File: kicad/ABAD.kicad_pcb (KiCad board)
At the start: 4 copper layers, 36.9 x 85.2 mm, 58 parts, among them J1 Edge mounted SMA, J2 USB_C_Receptacle_USB2.0_16P, J3 BATT Screw Terminal, Q1 AO3401A, Q2 AO3401A, U2 ESP32-S3-WROOM-1, U3 USBLC6-2SC6, U4 TPS63001, U6 MPU-6050, U7 MS5611-01BA, U8 L80-R

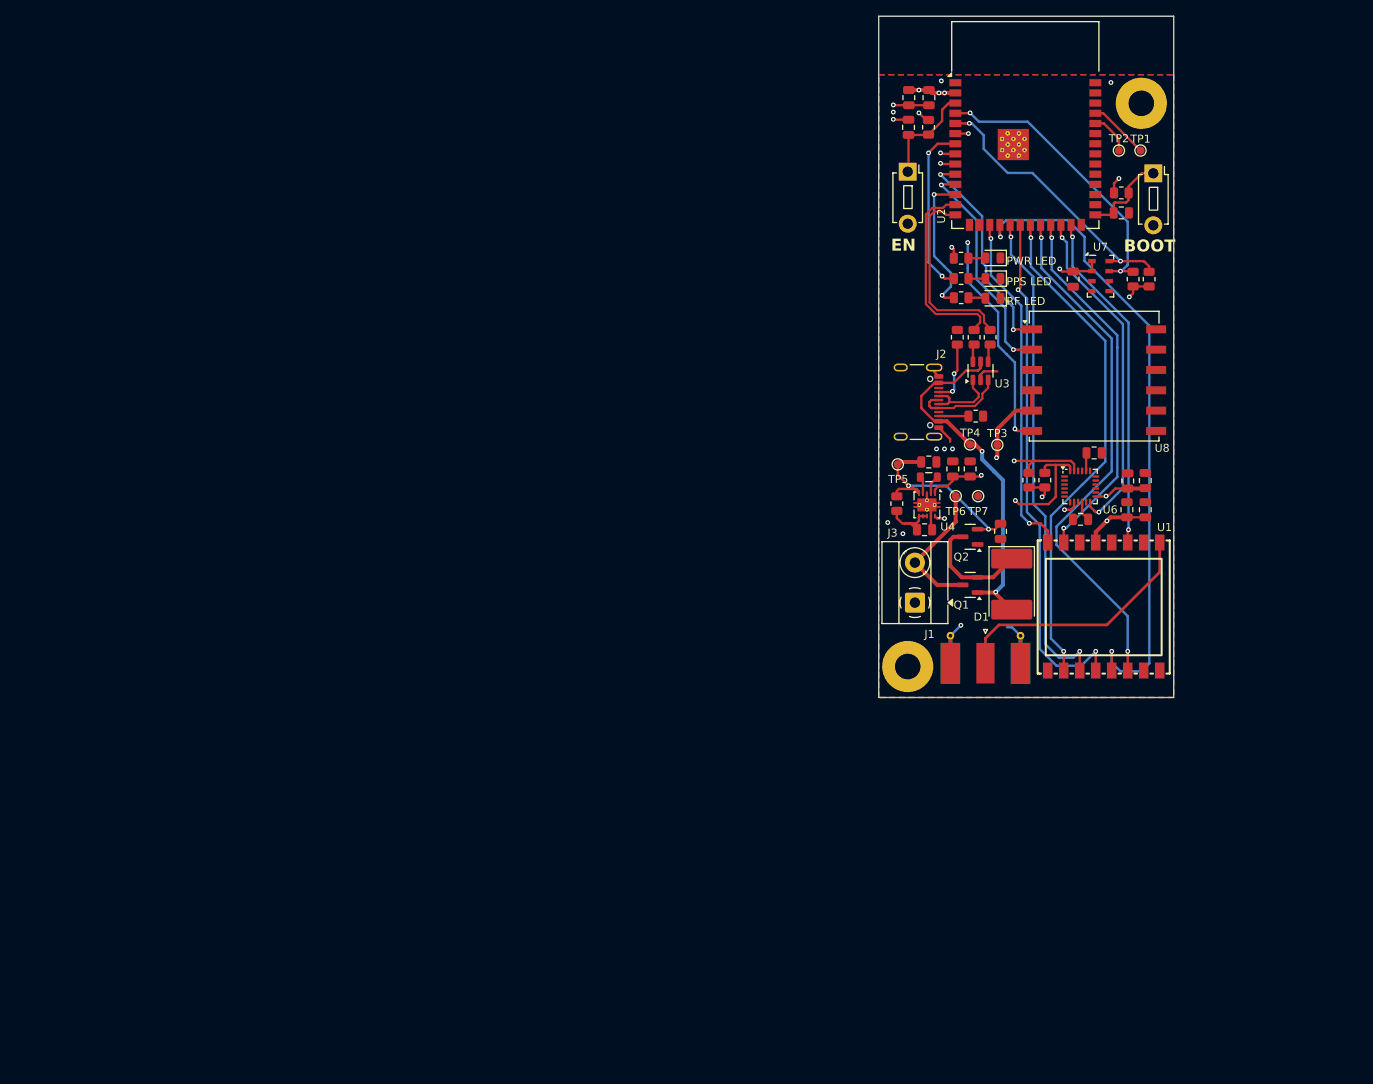
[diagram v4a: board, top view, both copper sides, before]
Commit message: Completed PCB + Sch, RP2040 based
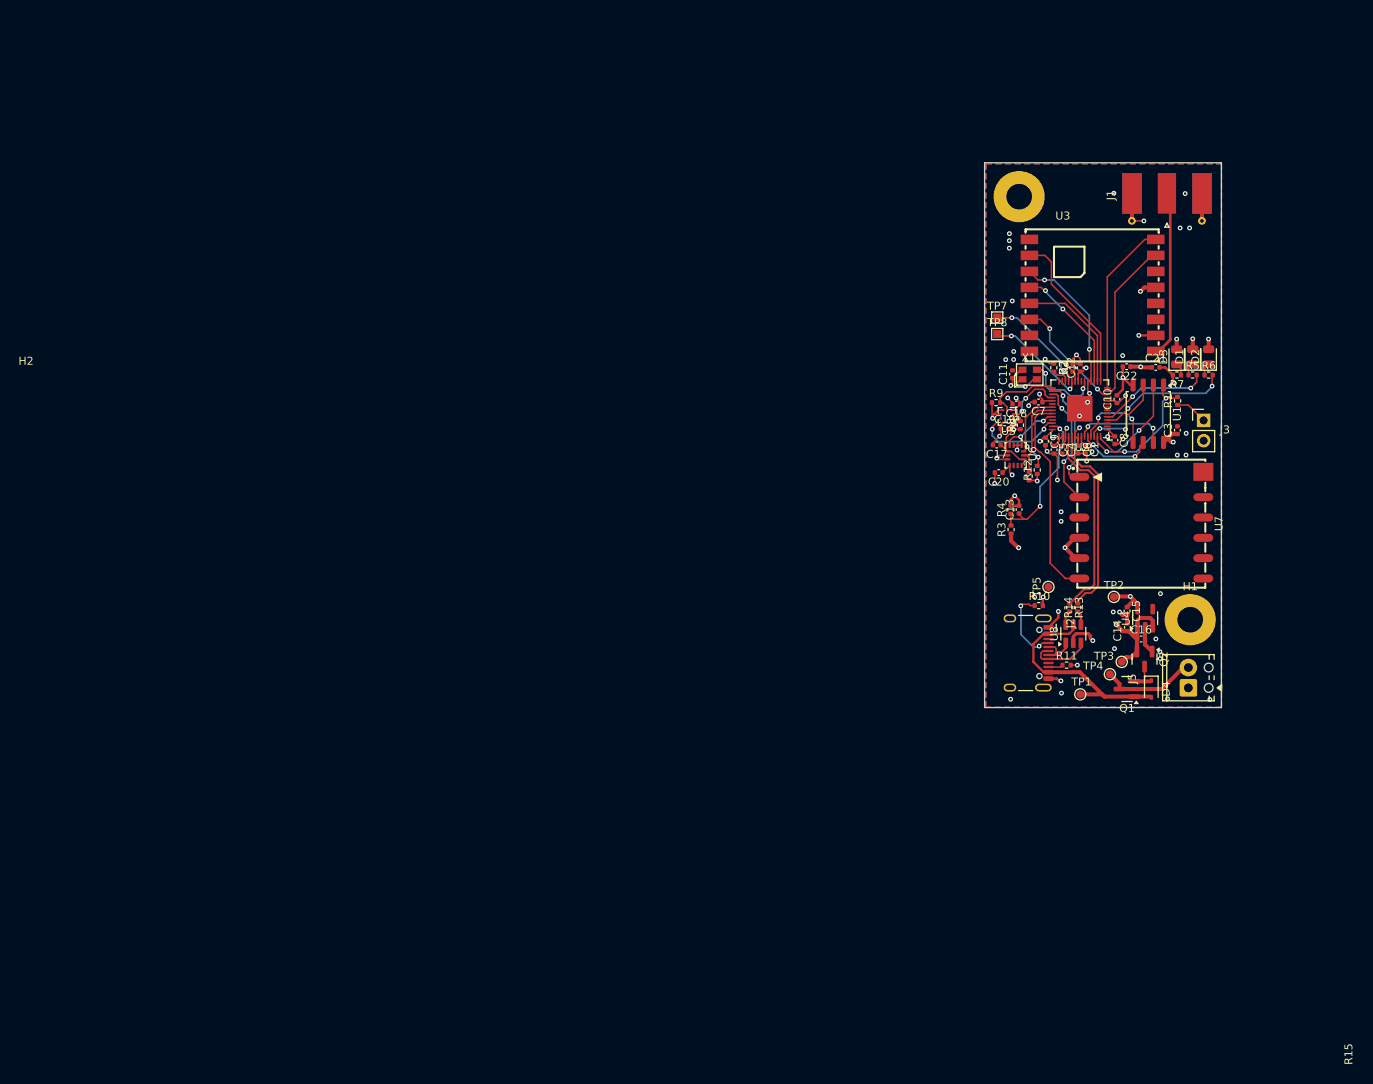
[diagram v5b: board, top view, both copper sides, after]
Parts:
- removed L1: 1.5A 2.2uH, Inductor_SMD:L_0805_2012Metric
- removed RESET_SW1, RESET_SW2: SW_Push, Button_Switch_THT:SW_PUSH_1P1T_6x3.5mm_H4.3_APEM_MJTP1243
- removed TP6: BATT_RAW+, TestPoint:TestPoint_Pad_D1.0mm
- added C19: 100nF, Capacitor_SMD:C_0402_1005Metric, F.Cu at (144.0, 94.9)
- added C20: 100nF, Capacitor_SMD:C_0402_1005Metric, F.Cu at (143.3, 100.4)
- added C21: 100nF, Capacitor_SMD:C_0402_1005Metric, F.Cu at (162.9, 87.2)
- added C22: 10uF, Capacitor_SMD:C_0402_1005Metric, F.Cu at (159.3, 87.1)
- added C5: 1uF, Capacitor_SMD:C_0402_1005Metric, F.Cu at (150.2, 97.5)
- added C6: 100nF, Capacitor_SMD:C_0402_1005Metric, F.Cu at (153.2, 97.5)
- added J5: BATT Screw Terminal, TerminalBlock_Phoenix:TerminalBlock_Phoenix_MPT-0,5-2-2.54_1x02_P2.54mm_Horizontal, F.Cu at (167.0, 127.3)
- added R15: 10k, Resistor_SMD:R_0402_1005Metric, F.Cu at (147.1, 100.8)
- added TP8: SWD, TestPoint:TestPoint_Pad_1.0x1.0mm, F.Cu at (143.1, 83.0)
- added U5: BMP390, JLC_BMP390:LGA-10_L2.0-W2.0-P0.50-TL_BMP390L, F.Cu at (144.3, 93.3)
- added X1: 12MHz, Crystal:OSC-SMD_4P-L2.0-W1.6-BL, F.Cu at (147.2, 88.1)
- C1: footprint Capacitor_SMD:C_0805_2012Metric -> Capacitor_SMD:C_0402_1005Metric
- C10, C11, C2, C9: value 10uF -> 100nF; footprint Capacitor_SMD:C_0805_2012Metric -> Capacitor_SMD:C_0402_1005Metric
- C12: value 10nF, 4V -> 100nF; footprint Capacitor_SMD:C_0805_2012Metric -> Capacitor_SMD:C_0402_1005Metric
- C13: value 0.1uF, 4V -> 100nF; footprint Capacitor_SMD:C_0805_2012Metric -> Capacitor_SMD:C_0402_1005Metric
- C14: value 100nF -> 1uF; footprint Capacitor_SMD:C_0805_2012Metric -> Capacitor_SMD:C_0402_1005Metric
- C15: value 0.1uF, 2V -> 1uF; footprint Capacitor_SMD:C_0805_2012Metric -> Capacitor_SMD:C_0402_1005Metric
- C16: value 2.2nF, 50V -> 10uF; footprint Capacitor_SMD:C_0805_2012Metric -> Capacitor_SMD:C_0402_1005Metric
- C17: value 22uF -> 100nF; footprint Capacitor_SMD:C_0805_2012Metric -> Capacitor_SMD:C_0402_1005Metric
- C18, C8: value 0.1uF -> 100nF; footprint Capacitor_SMD:C_0805_2012Metric -> Capacitor_SMD:C_0402_1005Metric
- C3: value 10uF 6.3V -> 100nF; footprint Capacitor_SMD:C_0805_2012Metric -> Capacitor_SMD:C_0402_1005Metric
- C4: value 0.1uF -> 1uF; footprint Capacitor_SMD:C_0805_2012Metric -> Capacitor_SMD:C_0402_1005Metric
- C7: value 1uF -> 100nF; footprint Capacitor_SMD:C_0805_2012Metric -> Capacitor_SMD:C_0402_1005Metric
- D1: value D_Schottky -> RF_LED_GREEN; footprint Diode_SMD:D_3220_8050Metric -> LED_SMD:LED_0805_2012Metric
- D2: value RF_LED_GREEN -> GPS_LED_BLUE
- D3: value GPS_LED_BLUE -> PWR_LED_RED
- D4: value PWR_LED_RED -> D_Schottky; footprint LED_SMD:LED_0805_2012Metric -> Diode_SMD:D_SOD-323
- J2: footprint Connector_USB:USB_C_Receptacle_GCT_USB4105-xx-A_16P_TopMnt_Horizontal -> Connector_USB:USB_C_Receptacle_HCTL_HC-TYPE-C-16P-01A
- J3: value BATT Screw Terminal -> Conn_01x02; footprint TerminalBlock_MetzConnect:TerminalBlock_MetzConnect_Type055_RT01502HDWU_1x02_P5.00mm_Horizontal -> Connector_PinHeader_2.54mm:PinHeader_1x02_P2.54mm_Vertical
- R1: value 5.1k -> 1k; footprint Resistor_SMD:R_0805_2012Metric -> Resistor_SMD:R_0402_1005Metric
- R10: value 68 -> 5.1k; footprint Resistor_SMD:R_0805_2012Metric -> Resistor_SMD:R_0402_1005Metric
- R11: value 10k -> 5.1k; footprint Resistor_SMD:R_0805_2012Metric -> Resistor_SMD:R_0402_1005Metric
- R12, R2: footprint Resistor_SMD:R_0805_2012Metric -> Resistor_SMD:R_0402_1005Metric
- R13, R14: value 10k -> 22Ω; footprint Resistor_SMD:R_0805_2012Metric -> Resistor_SMD:R_0402_1005Metric
- R3: value 100Ω -> 30k; footprint Resistor_SMD:R_0805_2012Metric -> Resistor_SMD:R_0402_1005Metric
- R4: value 22Ω -> 51k; footprint Resistor_SMD:R_0805_2012Metric -> Resistor_SMD:R_0402_1005Metric
- R5: value 22Ω -> 1k; footprint Resistor_SMD:R_0805_2012Metric -> Resistor_SMD:R_0402_1005Metric
- R6, R7: value 10k -> 1k; footprint Resistor_SMD:R_0805_2012Metric -> Resistor_SMD:R_0402_1005Metric
- R8, R9: value 68 -> 4.7k; footprint Resistor_SMD:R_0805_2012Metric -> Resistor_SMD:R_0402_1005Metric
- TP1: value TXD0 -> VBUS
- TP2: value RXD0 -> 3.3V
- TP3: value 3.3V -> BATT+
- TP4: value VBUS -> BATT_RAW+
- TP5: value BATT+ -> GND
- TP7: value GND -> SWCLK; footprint TestPoint:TestPoint_Pad_D1.0mm -> TestPoint:TestPoint_Pad_1.0x1.0mm
- U1: value ~ -> W25Q128JVS; footprint Lora1262:WIRELM-SMD_16P-L16.0-W16.0-P2.00_LORA-CC68-915MHZ-TCXO -> Package_SO:SOIC-8_5.3x5.3mm_P1.27mm
- U2: value ESP32-S3-WROOM-1 -> RP2040; footprint RF_Module:ESP32-S3-WROOM-1 -> Package_DFN_QFN:QFN-56-1EP_7x7mm_P0.4mm_EP3.2x3.2mm
- U3: value USBLC6-2SC6 -> 433MHz; footprint Package_TO_SOT_SMD:SOT-23-6 -> LORA-CC68-433MHz-TCXO:LCC-16_L16.0-W16.0-P2.00-TL
- U4: value TPS63001 -> AP2112K-3.3; footprint Package_SON:Texas_DRC0010J_ThermalVias -> Package_TO_SOT_SMD:SOT-23-5
- U6: value MPU-6050 -> LSMDSO32TR; footprint Sensor_Motion:InvenSense_QFN-24_4x4mm_P0.5mm -> LSMDSO32TR:LGA-14_L3.0-W2.5-P0.50-TL
- U7: value MS5611-01BA -> L80RE-M37; footprint Package_LGA:LGA-8_3x5mm_P1.25mm -> L80RE-M37:GPSM-SMD_12P-L16.0-W16.0-P2.54-BL
- U8: value L80-R -> USBLC6-2SC6; footprint RF_GPS:Quectel_L80-R -> Package_TO_SOT_SMD:SOT-23-6
- moved TP1 68.4 mm to (153.5, 128.1)
- moved J1 59.8 mm to (164.3, 67.2), turned to -90 degrees
- moved D4 57.4 mm to (162.3, 127.4), turned to -90 degrees
- moved TP2 55.8 mm to (157.7, 115.9)
- moved R11 49.0 mm to (151.8, 124.4), turned to 0 degrees
- moved R6 46.7 mm to (169.5, 88.2), turned to 0 degrees
- moved C17 44.8 mm to (143.0, 96.9), turned to 180 degrees
- moved R10 44.5 mm to (148.3, 117.0), turned to 0 degrees
- moved C14 44.1 mm to (159.4, 119.7), turned to 90 degrees
- moved J3 42.7 mm to (168.9, 93.8), turned to 0 degrees
- moved C18 39.8 mm to (145.5, 91.8), turned to 180 degrees
- moved C7 38.0 mm to (148.2, 91.5), turned to 180 degrees
- moved D1 36.3 mm to (167.5, 85.9), turned to 90 degrees
- moved U2 36.1 mm to (153.4, 92.4), turned to 180 degrees
- moved H1 35.8 mm to (167.2, 118.8)
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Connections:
- C1 pad 1: GND -> +1V1
- C1 pad 2: +3.3V -> GND
- C10 pad 1: +BATT -> +3V3
- C11 pad 1: +3.3V -> +3V3
- C12 pad 1: GND -> +3V3
- C12 pad 2: +3.3V -> GND
- C13 pad 1: +3.3V -> /BATT SENSE
- C14 pad 1: +3.3V -> +BATT
- C15 pad 1: Net-(U6-REGOUT) -> +3V3
- C16 pad 1: Net-(U6-CPOUT) -> +BATT
- C17 pad 1: GND -> +3V3
- C17 pad 2: +3.3V -> GND
- C18 pad 2: +3.3V -> +3V3
- C2 pad 1: GND -> +1V1
- C2 pad 2: +3.3V -> GND
- C3 pad 1: +BATT -> +3V3
- C4 pad 1: Net-(U4-EN) -> +1V1
- C7 pad 1: GND -> +3V3
- C7 pad 2: /EN_RST -> GND
- C8 pad 1: GND -> +3V3
- C8 pad 2: /BOOT -> GND
- C9 pad 1: +3.3V -> +3V3
- D1 pad 2: VBUS -> +3V3
- D2 pad 1: GND -> Net-(D2-K)
- D2 pad 2: Net-(D2-A) -> +3V3
- D3 pad 1: GND -> Net-(D3-K)
- D3 pad 2: Net-(D3-A) -> +3V3
- D4 pad 1: GND -> Net-(D4-K)
- D4 pad 2: Net-(D4-A) -> VBUS
- J2 pad A6: USB+ -> Net-(J2-D+-PadA6)
- J2 pad A7: USB- -> Net-(J2-D--PadA7)
- J2 pad B6: USB+ -> Net-(J2-D+-PadA6)
- J2 pad B7: USB- -> Net-(J2-D--PadA7)
- J3 pad 1: GND -> /BOOTSEL
- J3 pad 2: BATT_RAW+ -> GND
- Q1 pad 2: Net-(D1-K) -> Net-(D4-K)
- Q1 pad 3: BATT_RAW+ -> RAW_BATT+
- Q2 pad 3: Net-(D1-K) -> Net-(D4-K)
- R1 pad 1: Net-(J2-CC1) -> /BOOTSEL
- R1 pad 2: GND -> /QSPI_SS
- R10 pad 1: Net-(D4-A) -> Net-(J2-CC1)
- R10 pad 2: +3.3V -> GND
- R11 pad 1: +3.3V -> Net-(J2-CC2)
- R11 pad 2: /BARO_SDA -> GND
- R12 pad 1: +3.3V -> +3V3
- R12 pad 2: /BARO_SCL -> /ACCEL_SDA
- R13 pad 1: +3.3V -> /USB_D-
- R13 pad 2: /ACCEL_SDA -> Net-(R13-Pad2)
- R14 pad 1: +3.3V -> Net-(R14-Pad1)
- R14 pad 2: /ACCEL_SCL -> /USB_D+
- R2 pad 1: Net-(J2-CC2) -> +3V3
- R2 pad 2: GND -> /RUN
- R3 pad 2: Net-(U4-EN) -> /BATT SENSE
- R4 pad 1: USBN -> /BATT SENSE
- R4 pad 2: Net-(R4-Pad2) -> GND
- R5 pad 1: Net-(R5-Pad1) -> Net-(D1-K)
- R5 pad 2: USBP -> /RF_LED
- R6 pad 1: /EN_RST -> Net-(D2-K)
- R6 pad 2: +3.3V -> /PPS_LED
- R7 pad 1: /BOOT -> Net-(D3-K)
- R7 pad 2: +3.3V -> GND
- R8 pad 1: Net-(D2-A) -> +3V3
- R8 pad 2: /RF_LED -> /BMP_SCL
- R9 pad 1: Net-(D3-A) -> +3V3
- R9 pad 2: /PPS_LED -> /BMP_SDA
- TP1 pad 1: /TXD0 -> VBUS
- TP2 pad 1: /RXD0 -> +3V3
- TP3 pad 1: +3.3V -> +BATT
- TP4 pad 1: VBUS -> RAW_BATT+
- TP5 pad 1: +BATT -> GND
- TP7 pad 1: GND -> /SWD
- U1 pad 1: GND -> /QSPI_SS
- U1 pad 2: /MISO -> /QSPI_SD1
- U1 pad 3: /MOSI -> /QSPI_SD2
- U1 pad 4: /SCLK -> GND
- U1 pad 5: /NSS -> /QSPI_SD0
- U1 pad 6: /NRESET -> /QSPI_SCLK
- U1 pad 7: unconnected-(U1-NC-Pad7) -> /QSPI_SD3
- U1 pad 8: GND -> +3V3
- U2 pad 1: GND -> +3V3
- U2 pad 10: /GPS_RX -> +3V3
- U2 pad 11: /GPS_TX -> unconnected-(U2-GPIO8-Pad11)
- U2 pad 12: /RF_LED -> /RESET
- U2 pad 13: USBN -> /DIO1
- U2 pad 14: USBP -> /BUSY
- U2 pad 15: unconnected-(U2-IO3-Pad15) -> /MISO
- U2 pad 16: unconnected-(U2-IO46-Pad16) -> /NSS
- U2 pad 17: /BUSY -> /SCK
- U2 pad 18: /NSS -> /MOSI
- U2 pad 19: /MOSI -> GND
- U2 pad 2: +3.3V -> unconnected-(U2-GPIO0-Pad2)
- U2 pad 20: /SCLK -> /XIN
- U2 pad 21: /MISO -> unconnected-(U2-XOUT-Pad21)
- U2 pad 22: /NRESET -> +3V3
- U2 pad 23: /TXCO -> +1V1
- U2 pad 24: /ACCEL_INT -> /SWCLK
- U2 pad 25: /RF_INT -> /SWD
- U2 pad 26: unconnected-(U2-IO45-Pad26) -> /RUN
- U2 pad 27: /BOOT -> unconnected-(U2-GPIO16-Pad27)
- U2 pad 29: unconnected-(U2-IO36-Pad29) -> /BMP_SDA
- U2 pad 3: /EN_RST -> unconnected-(U2-GPIO1-Pad3)
- U2 pad 30: unconnected-(U2-IO37-Pad30) -> /GPS_RX
- U2 pad 31: unconnected-(U2-IO38-Pad31) -> /GPS_TX
- U2 pad 32: unconnected-(U2-IO39-Pad32) -> /BMP_SCL
- U2 pad 33: unconnected-(U2-IO40-Pad33) -> +3V3
- U2 pad 35: unconnected-(U2-IO42-Pad35) -> /ACCEL_SDA
- U2 pad 36: /RXD0 -> /ACCEL_SCL
- U2 pad 37: /TXD0 -> /PPS
- U2 pad 38: unconnected-(U2-IO2-Pad38) -> /ACCEL_INT
- U2 pad 4: /BARO_SDA -> /PPS_LED
- U2 pad 40: GND -> /BMP_INT
- U2 pad 41: GND -> /BATT SENSE
- U2 pad 5: /BARO_SCL -> /RF_LED
- U2 pad 6: /PPS -> unconnected-(U2-GPIO4-Pad6)
- U2 pad 7: /PPS_LED -> unconnected-(U2-GPIO5-Pad7)
- U2 pad 8: /ACCEL_SDA -> unconnected-(U2-GPIO6-Pad8)
- U2 pad 9: /ACCEL_SCL -> unconnected-(U2-GPIO7-Pad9)
- U3 pad 1: USB- -> GND
- U3 pad 2: GND -> /MISO
- U3 pad 3: USB+ -> /MOSI
- U3 pad 4: Net-(R5-Pad1) -> /SCK
- U3 pad 5: VBUS -> /NSS
- U3 pad 6: Net-(R4-Pad2) -> /RESET
- U4 pad 1: +3.3V -> +BATT
- U4 pad 2: Net-(U4-L2) -> GND
- U4 pad 3: GND -> +BATT
- U4 pad 4: Net-(U4-L1) -> unconnected-(U4-NC-Pad4)
- U4 pad 5: +BATT -> +3V3
- U6 pad 1: unconnected-(U6-CLKIN-Pad1) -> GND
- U6 pad 10: Net-(U6-REGOUT) -> unconnected-(U6-NC-Pad10)
- U6 pad 11: GND -> unconnected-(U6-NC-Pad11)
- U6 pad 12: /ACCEL_INT -> +3V3
- U6 pad 13: +3.3V -> /ACCEL_SCL
- U6 pad 14: unconnected-(U6-NC-Pad14) -> /ACCEL_SDA
- U6 pad 2: unconnected-(U6-NC-Pad2) -> GND
- U6 pad 3: unconnected-(U6-NC-Pad3) -> GND
- U6 pad 4: unconnected-(U6-NC-Pad4) -> /ACCEL_INT
- U6 pad 5: unconnected-(U6-NC-Pad5) -> +3V3
- U6 pad 6: unconnected-(U6-AUX_DA-Pad6) -> GND
- U6 pad 7: unconnected-(U6-AUX_CL-Pad7) -> GND
- U6 pad 8: +3.3V -> +3V3
- U6 pad 9: GND -> unconnected-(U6-INT2-Pad9)
- U7 pad 1: +3.3V -> /GPS_RX
- U7 pad 2: +3.3V -> /GPS_TX
- U7 pad 4: GND -> +3V3
- U7 pad 5: GND -> +3V3
- U7 pad 6: unconnected-(U7-SDO-Pad6) -> /PPS
- U7 pad 7: /BARO_SDA -> unconnected-(U7-RESERVED-Pad7)
- U7 pad 8: /BARO_SCL -> unconnected-(U7-RESERVED-Pad8)
- U8 pad 1: /GPS_RX -> Net-(J2-D--PadA7)
- U8 pad 2: /GPS_TX -> GND
- U8 pad 3: GND -> Net-(J2-D+-PadA6)
- U8 pad 4: +3.3V -> Net-(R14-Pad1)
- U8 pad 5: +3.3V -> VBUS
- U8 pad 6: /PPS -> Net-(R13-Pad2)
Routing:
- net /ACCEL_SDA: track 81.3 -> 11.6 mm
- net +3V3: track 0.00 -> 69.5 mm, vias 0 -> 21
- net /NRESET: track 65.9 -> 0.00 mm, vias 2 -> 0
- net /SCLK: track 65.3 -> 0.00 mm, vias 2 -> 0
- net /NSS: track 80.7 -> 15.9 mm, vias 2 -> 0
- net +3.3V: track 60.8 -> 0.00 mm, vias 15 -> 0
- net /TXCO: track 46.1 -> 0.00 mm, vias 2 -> 0
- net /MOSI: track 62.0 -> 18.1 mm
- net /ACCEL_SCL: track 54.5 -> 11.1 mm, vias 2 -> 0
- net /RF_INT: track 42.7 -> 0.00 mm, vias 2 -> 0
- net /MISO: track 63.1 -> 20.6 mm, vias 2 -> 0
- net /BARO_SDA: track 36.9 -> 0.00 mm, vias 2 -> 0
- net GND: track 28.9 -> 64.2 mm, vias 11 -> 54
- net /ACCEL_INT: track 42.3 -> 7.15 mm
- net /BARO_SCL: track 34.7 -> 0.00 mm, vias 2 -> 0
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- added copper zone on In2.Cu, net +3V3
- removed copper zone on In2.Cu, net +3.3V
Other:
- board size 36.9 x 85.2 mm -> 29.6 x 68.1 mm
- board text removed: "BOOT"
- board text removed: "EN"
- board text removed: "PPS LED"
- board text removed: "PWR LED"
- board text removed: "RF LED"
